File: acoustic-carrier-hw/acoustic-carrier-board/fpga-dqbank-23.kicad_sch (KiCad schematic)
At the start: 13 parts, among them IC1 ECP5-BGA256

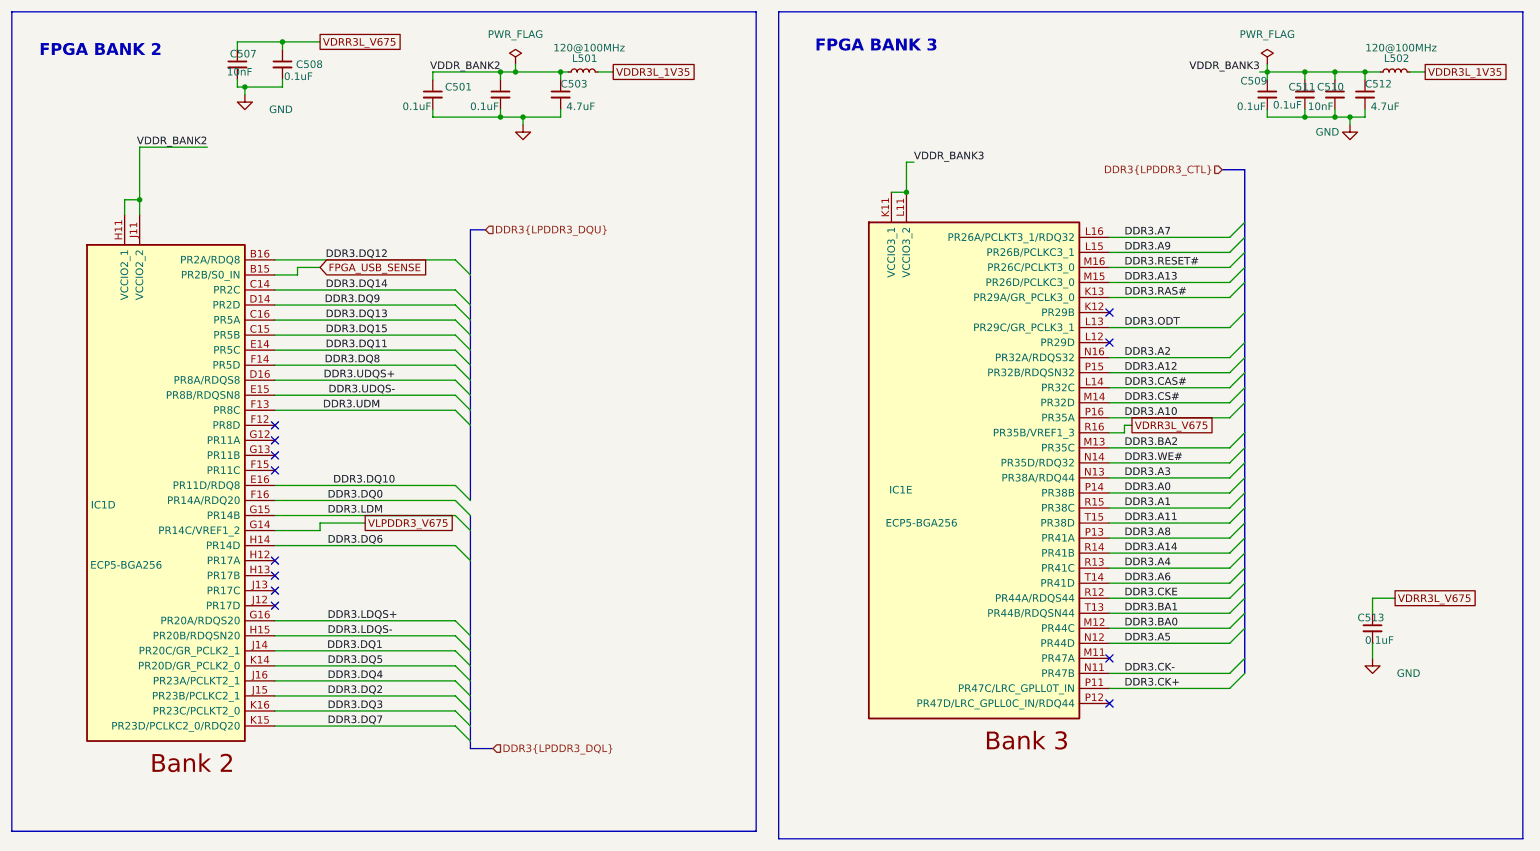
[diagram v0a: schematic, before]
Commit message: [carrier] Added 2 buttons and 2 leds + routing
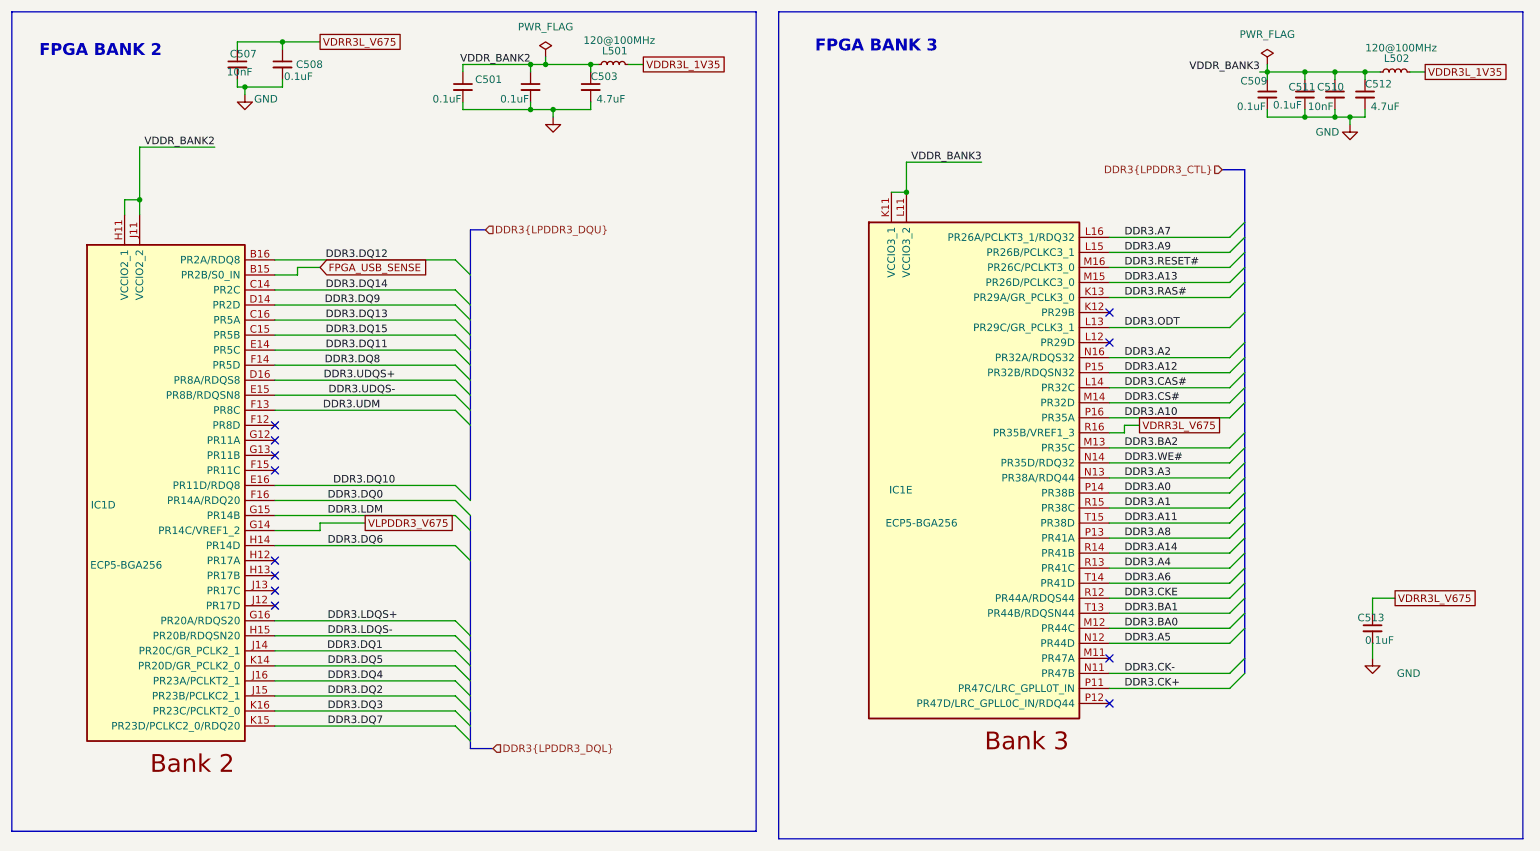
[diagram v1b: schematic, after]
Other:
- moved on the sheet: C501, C503, L501

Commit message: [carrier] Added decoupling to LPDDR3 and routed VREF (next) finalize power supply
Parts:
- removed L501, L502: 120@100MHz, Inductor_SMD:L_0603_1608Metric, symbol Device:L_Small
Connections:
- net VDDR_BANK3 is gone; now on net VLPDDR3_1V35: C509.1, C510.1, C511.1, C512.1, IC1.K11 (VCCIO3_1), IC1.L11 (VCCIO3_2)
- net VLPDDR3_V675: now also C507.1, C508.1, C513.1
- net VDDR_BANK2 renamed VLPDDR3_1V35
- removed net VDRR3L_V675: C507.1, C508.1, C513.1, IC1.R16 (PR35B/VREF1_3)
- new net VLPDDR3L_V675: IC1.R16 (PR35B/VREF1_3)
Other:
- moved on the sheet: C509, C510, C511, C512, C513

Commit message: [carrier] Further routing, ground plane removal underneath connectors, ..
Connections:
- net VLPDDR3L_V675 is gone; now on net VLPDDR3_V675: IC1.R16 (PR35B/VREF1_3)
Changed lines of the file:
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@@
 		)
 	)
-	(global_label "VLPDDR3L_V675"
+	(global_label "VLPDDR3_V675"
 		(shape passive)
 		(at 217.17 90.17 0)
@@
 		)
 		(property "Intersheetrefs" "${INTERSHEET_REFS}"
-			(at 234.1629 90.17 0)
+			(at 233.1348 90.17 0)
 			(effects
 				(font
